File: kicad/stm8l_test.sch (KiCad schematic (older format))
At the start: 39 parts, among them J1 Conn_01x04, J2 Conn_01x02, SW1 SW_Push, SW2 Rotary_Encoder_Switch, U1 STM8L101F3P

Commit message: stuff
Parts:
- BZ1: renamed from BZ?; footprint (none) -> Buzzer_Beeper:Buzzer_12x9.5RM7.6
- C1, C4: renamed from C?; footprint (none) -> Capacitor_SMD:C_0805_2012Metric_Pad1.18x1.45mm_HandSolder
- C2: renamed from C1; footprint (none) -> Capacitor_SMD:C_0603_1608Metric_Pad1.08x0.95mm_HandSolder
- C3: renamed from C2; footprint (none) -> Capacitor_SMD:C_0805_2012Metric_Pad1.18x1.45mm_HandSolder
- D1: renamed from D8; footprint (none) -> LED_SMD:LED_1206_3216Metric_Pad1.42x1.75mm_HandSolder
- D10: renamed from D?; footprint (none) -> LED_SMD:LED_1206_3216Metric_Pad1.42x1.75mm_HandSolder
- D2: renamed from D1; footprint (none) -> LED_SMD:LED_1206_3216Metric_Pad1.42x1.75mm_HandSolder
- D3: renamed from D2; footprint (none) -> LED_SMD:LED_1206_3216Metric_Pad1.42x1.75mm_HandSolder
- D4: renamed from D3; footprint (none) -> LED_SMD:LED_1206_3216Metric_Pad1.42x1.75mm_HandSolder
- D5: renamed from D4; footprint (none) -> LED_SMD:LED_1206_3216Metric_Pad1.42x1.75mm_HandSolder
- D6: renamed from D?; footprint (none) -> Diode_SMD:D_1210_3225Metric_Pad1.42x2.65mm_HandSolder
- D7: renamed from D5; footprint (none) -> LED_SMD:LED_1206_3216Metric_Pad1.42x1.75mm_HandSolder
- D8: renamed from D6; footprint (none) -> LED_SMD:LED_1206_3216Metric_Pad1.42x1.75mm_HandSolder
- D9: renamed from D7; footprint (none) -> LED_SMD:LED_1206_3216Metric_Pad1.42x1.75mm_HandSolder
- J1: footprint (none) -> Connector_PinHeader_2.54mm:PinHeader_1x04_P2.54mm_Vertical
- J2: footprint (none) -> TerminalBlock_Phoenix:TerminalBlock_Phoenix_PT-1,5-2-5.0-H_1x02_P5.00mm_Horizontal
- J3: renamed from J?; symbol Connector:USB_B_Micro -> stm8l_test-rescue:USB_B_Micro-Connector
- J4: renamed from J?; footprint (none) -> Connector_PinHeader_2.00mm:PinHeader_1x02_P2.00mm_Vertical
- L1: renamed from L?; footprint (none) -> Inductor_SMD:L_Wuerth_WE-PD-Typ-7345
- R1: footprint (none) -> Resistor_SMD:R_0603_1608Metric_Pad0.98x0.95mm_HandSolder
- R10: renamed from R7; footprint (none) -> Resistor_SMD:R_0603_1608Metric_Pad0.98x0.95mm_HandSolder
- R11: renamed from R8; footprint (none) -> Resistor_SMD:R_0603_1608Metric_Pad0.98x0.95mm_HandSolder
- R12, R2, R8: renamed from R?; footprint (none) -> Resistor_SMD:R_0603_1608Metric_Pad0.98x0.95mm_HandSolder
- R3: renamed from R9; footprint (none) -> Resistor_SMD:R_0603_1608Metric_Pad0.98x0.95mm_HandSolder
- R4: renamed from R2; footprint (none) -> Resistor_SMD:R_0603_1608Metric_Pad0.98x0.95mm_HandSolder
- R5: renamed from R3; footprint (none) -> Resistor_SMD:R_0603_1608Metric_Pad0.98x0.95mm_HandSolder
- R6: renamed from R4; footprint (none) -> Resistor_SMD:R_0603_1608Metric_Pad0.98x0.95mm_HandSolder
- R7: renamed from R5; footprint (none) -> Resistor_SMD:R_0603_1608Metric_Pad0.98x0.95mm_HandSolder
- R9: renamed from R6; footprint (none) -> Resistor_SMD:R_0603_1608Metric_Pad0.98x0.95mm_HandSolder
- SW1: footprint (none) -> Button_Switch_THT:SW_PUSH_6mm
- SW2: renamed from SW?; footprint (none) -> Connector_PinSocket_2.54mm:PinSocket_1x03_P2.54mm_Vertical
- SW3: renamed from SW2; footprint (none) -> Rotary_Encoder:RotaryEncoder_Alps_EC11E-Switch_Vertical_H20mm
- U3: renamed from U?; symbol random_things:BD70522GUL-E2 -> stm8l_test-rescue:BD70522GUL-E2-random_things
- gave numbers to parts that had none: 2
- renumbered U1 to U2
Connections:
- wire segments 29 -> 30
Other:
- moved on the sheet: BZ1, C1, C2, C3, C4, D1, D10, D2, D3, D4, D5, D6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

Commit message: Rev1 deb pcb
eta ets not stronk
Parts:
- removed D1: green, LED_SMD:LED_1206_3216Metric_Pad1.42x1.75mm_HandSolder, symbol Device:LED_Small
- removed J3: USB_B_Micro, symbol stm8l_test-rescue:USB_B_Micro-Connector
- removed J4: bat, Connector_PinHeader_2.00mm:PinHeader_1x02_P2.00mm_Vertical, symbol Connector_Generic:Conn_01x02
- removed R10, R11, R12, R4, R5, R6, R7, R9: 330, Resistor_SMD:R_0603_1608Metric_Pad0.98x0.95mm_HandSolder, symbol Device:R_Small
- removed R3: 1k, Resistor_SMD:R_0603_1608Metric_Pad0.98x0.95mm_HandSolder, symbol Device:R_Small
- removed U1: MCP73832-2-OT, Package_TO_SOT_SMD:SOT-23-5, symbol Battery_Management:MCP73832-2-OT
- removed U3: BD70522GUL-E2, symbol stm8l_test-rescue:BD70522GUL-E2-random_things
- added U3: BD70522GUL-E2, good_things:BGA-9_3x3_1.76x1.56mm, symbol good_things:BD70522GUL-E2
- BZ1: footprint Buzzer_Beeper:Buzzer_12x9.5RM7.6 -> good_things:buzzer_d14_p5
- C1, C3, C4: footprint Capacitor_SMD:C_0805_2012Metric_Pad1.18x1.45mm_HandSolder -> Capacitor_SMD:C_0805_2012Metric_Pad1.15x1.40mm_HandSolder
- C2: footprint Capacitor_SMD:C_0603_1608Metric_Pad1.08x0.95mm_HandSolder -> Capacitor_SMD:C_0603_1608Metric_Pad1.05x0.95mm_HandSolder
- R1: value R_Small -> 10k; footprint Resistor_SMD:R_0603_1608Metric_Pad0.98x0.95mm_HandSolder -> Resistor_SMD:R_0603_1608Metric_Pad1.05x0.95mm_HandSolder
- R2: value 2k -> 1k; footprint Resistor_SMD:R_0603_1608Metric_Pad0.98x0.95mm_HandSolder -> Resistor_SMD:R_0603_1608Metric_Pad1.05x0.95mm_HandSolder
- R8: footprint Resistor_SMD:R_0603_1608Metric_Pad0.98x0.95mm_HandSolder -> Resistor_SMD:R_0603_1608Metric_Pad1.05x0.95mm_HandSolder
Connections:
- net labels added: 1v8
- net labels removed: +5V, 2v5, charge
- wire segments 30 -> 27
- no-connect marks 9 -> 5
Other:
- moved on the sheet: BZ1, D10, D2, D3, D4, D5, D6, D7, D8, D9, Q1, R8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

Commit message: thinking about the solution, picking leds et al
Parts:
- removed C1: 10u, Capacitor_SMD:C_0805_2012Metric_Pad1.15x1.40mm_HandSolder, symbol Device:C_Small
- removed C4: 22u, Capacitor_SMD:C_0805_2012Metric_Pad1.15x1.40mm_HandSolder, symbol Device:C_Small
- removed D10, D8, D9: red, LED_SMD:LED_1206_3216Metric_Pad1.42x1.75mm_HandSolder, symbol Device:LED_Small
- removed L1: 2u2, Inductor_SMD:L_Wuerth_WE-PD-Typ-7345, symbol Device:L_Small
- removed R1: 10k, Resistor_SMD:R_0603_1608Metric_Pad1.05x0.95mm_HandSolder, symbol Device:R_Small
- removed U3: BD70522GUL-E2, good_things:BGA-9_3x3_1.76x1.56mm, symbol good_things:BD70522GUL-E2
- added D? (x20): red, LED_SMD:LED_1206_3216Metric_Pad1.42x1.75mm_HandSolder, symbol Device:LED_Small
- added F?: 500ma, symbol Device:Fuse_Small
- added Q? (x6): SI2365EDS-T1-GE3, symbol Device:Q_PMOS_GSD
- added R?: 1k, symbol Device:R_Small
- D7: value red -> VLMO30L1M2-GS18
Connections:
- net labels added: a0, a1, a2, a3, a4, c0, c1, c2, c3, c4, c5, pa0
- net labels removed: 1v8, b0, b1, b2, b3, b4, b5, b6, b7, encoder_sw, swim_data
- wire segments 27 -> 88
- no-connect marks 5 -> 2
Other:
- moved on the sheet: BZ1, C2, C3, D2, D3, D4, D5, D6, D7, J1, J2, Q1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

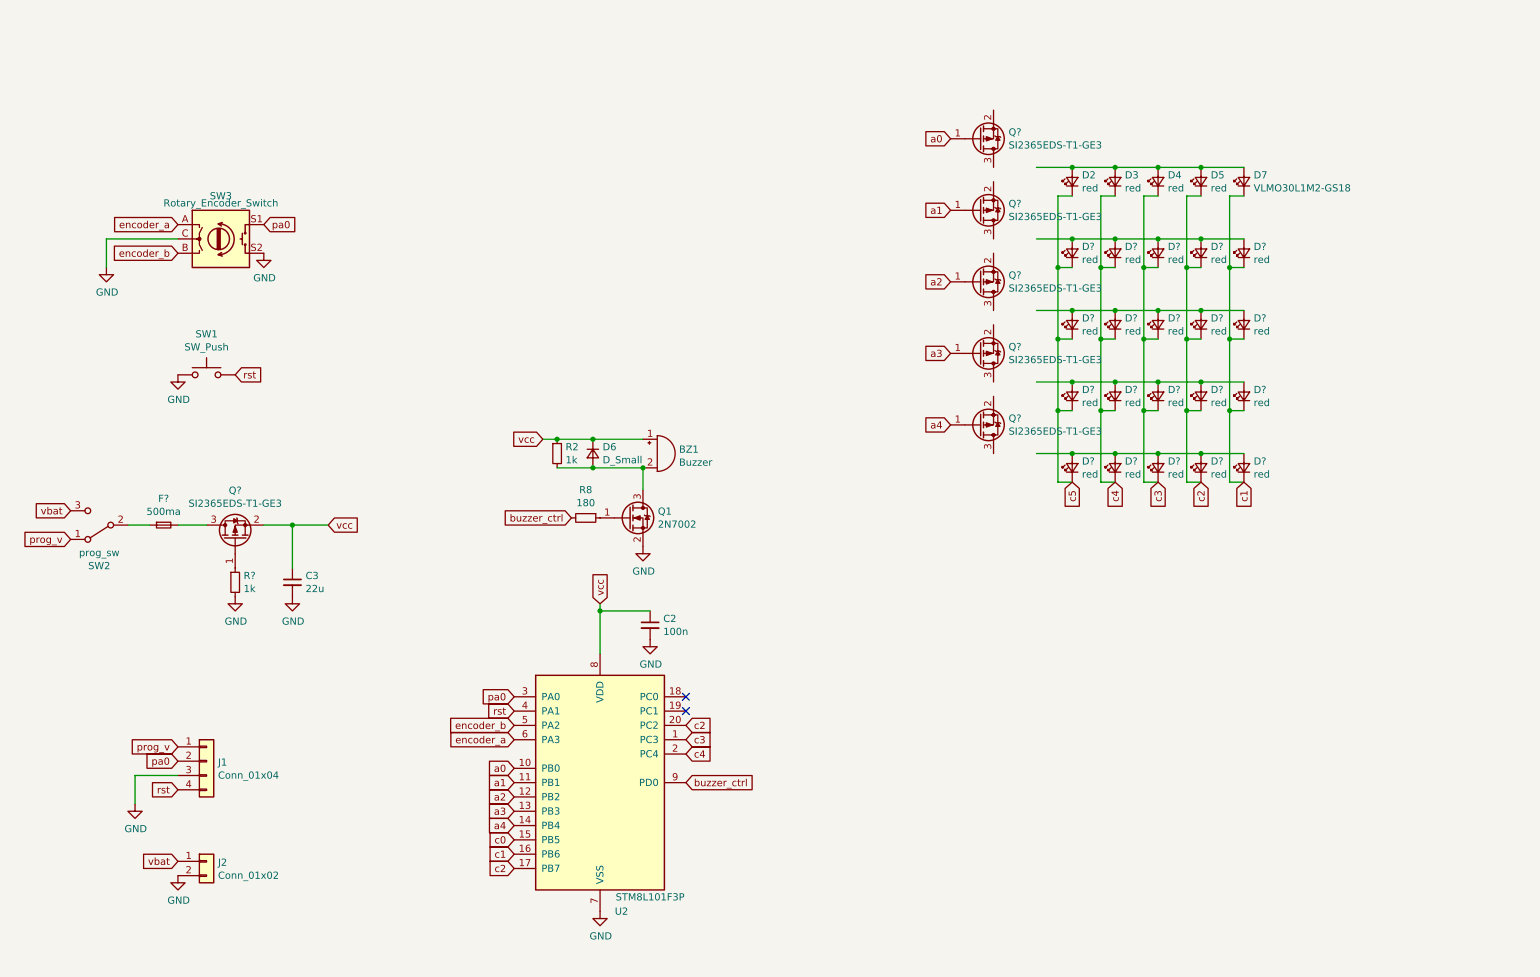
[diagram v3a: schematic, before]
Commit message: Pdb work, schema done
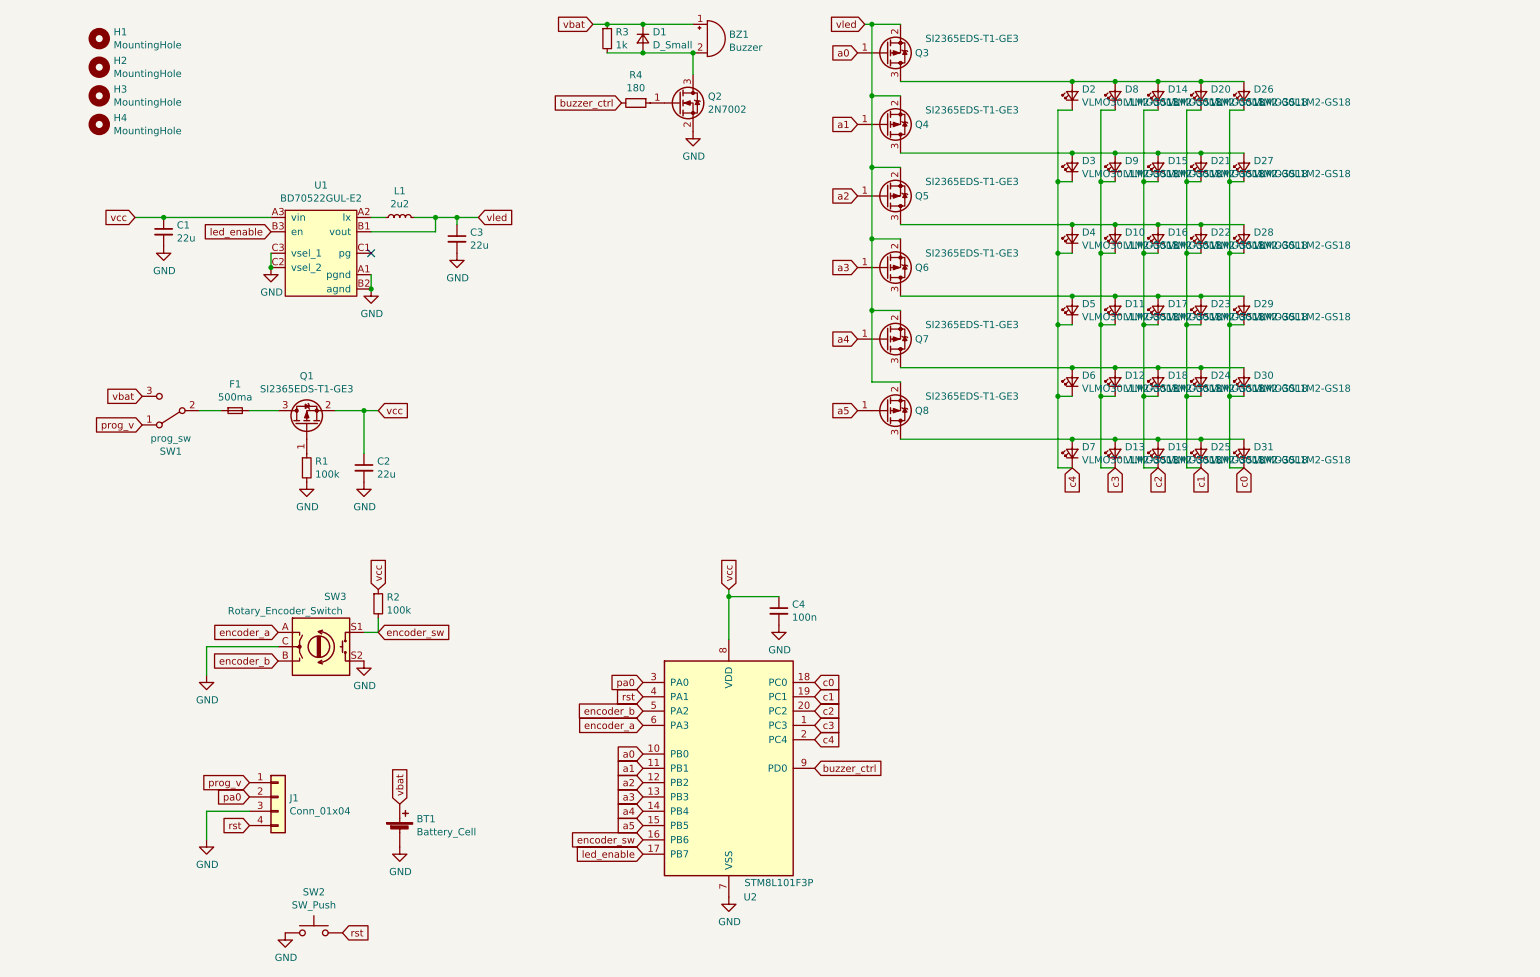
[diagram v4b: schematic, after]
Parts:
- removed D? (x20): red, LED_SMD:LED_1206_3216Metric_Pad1.42x1.75mm_HandSolder, symbol Device:LED_Small
- removed J2: Conn_01x02, TerminalBlock_Phoenix:TerminalBlock_Phoenix_PT-1,5-2-5.0-H_1x02_P5.00mm_Horizontal, symbol Connector_Generic:Conn_01x02
- removed Q? (x5): SI2365EDS-T1-GE3, symbol Device:Q_PMOS_GSD
- added BT1: Battery_Cell, Battery:BatteryHolder_Keystone_3002_1x2032, symbol Device:Battery_Cell
- added C1, C3: 22u, Capacitor_SMD:C_0603_1608Metric_Pad1.05x0.95mm_HandSolder, symbol Device:C_Small
- added D10, D11, D12, D13, D14, D15, D16, D17, D18, D19, D20, D21, D22, D23, D24, D25, D27, D28, D29, D30, D31, D6, D7, D8, D9: VLMO30L1M2-GS18, LED_SMD:LED_PLCC-2, symbol Device:LED_Small
- added H1, H2, H3, H4: MountingHole, MountingHole:MountingHole_2.7mm_M2.5, symbol Mechanical:MountingHole
- added L1: 2u2, Inductor_SMD:L_Wuerth_WE-PD-Typ-7345, symbol Device:L_Small
- added Q3, Q4, Q5, Q6, Q7, Q8: SI2365EDS-T1-GE3, Package_TO_SOT_SMD:SOT-23_Handsoldering, symbol Device:Q_PMOS_GSD
- added R2: 100k, Resistor_SMD:R_0603_1608Metric_Pad1.05x0.95mm_HandSolder, symbol Device:R_Small
- added U1: BD70522GUL-E2, good_things:BGA-9_3x3_1.76x1.56mm, symbol good_things:BD70522GUL-E2
- C2: renamed from C3; footprint Capacitor_SMD:C_0805_2012Metric_Pad1.15x1.40mm_HandSolder -> Capacitor_SMD:C_0603_1608Metric_Pad1.05x0.95mm_HandSolder
- D2, D3, D4, D5: value red -> VLMO30L1M2-GS18; footprint LED_SMD:LED_1206_3216Metric_Pad1.42x1.75mm_HandSolder -> LED_SMD:LED_PLCC-2
- D26: renamed from D7; footprint LED_SMD:LED_1206_3216Metric_Pad1.42x1.75mm_HandSolder -> LED_SMD:LED_PLCC-2
- F1: renamed from F?; footprint (none) -> Fuse:Fuse_1206_3216Metric_Pad1.42x1.75mm_HandSolder
- J1: footprint Connector_PinHeader_2.54mm:PinHeader_1x04_P2.54mm_Vertical -> good_things:TSM-104-01-L-SH
- Q1: renamed from Q?; footprint (none) -> Package_TO_SOT_SMD:SOT-23_Handsoldering
- R1: renamed from R?; value 1k -> 100k; footprint (none) -> Resistor_SMD:R_0603_1608Metric_Pad1.05x0.95mm_HandSolder
- SW1: renamed from SW2; footprint Connector_PinSocket_2.54mm:PinSocket_1x03_P2.54mm_Vertical -> good_things:TSM-103-01-l_SH
- SW2: renamed from SW1; footprint Button_Switch_THT:SW_PUSH_6mm -> good_things:push_sw_purple
- renumbered C2 to C4, D6 to D1, Q1 to Q2, R2 to R3, R8 to R4
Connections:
- net labels added: a5, encoder_sw, led_enable, vled
- net labels removed: c5
- wire segments 88 -> 128
- no-connect marks 2 -> 1
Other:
- moved on the sheet: BZ1, C2, C4, D1, D26, F1, J1, Q1, Q2, R1, R3, R4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

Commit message: Place components and initial routing
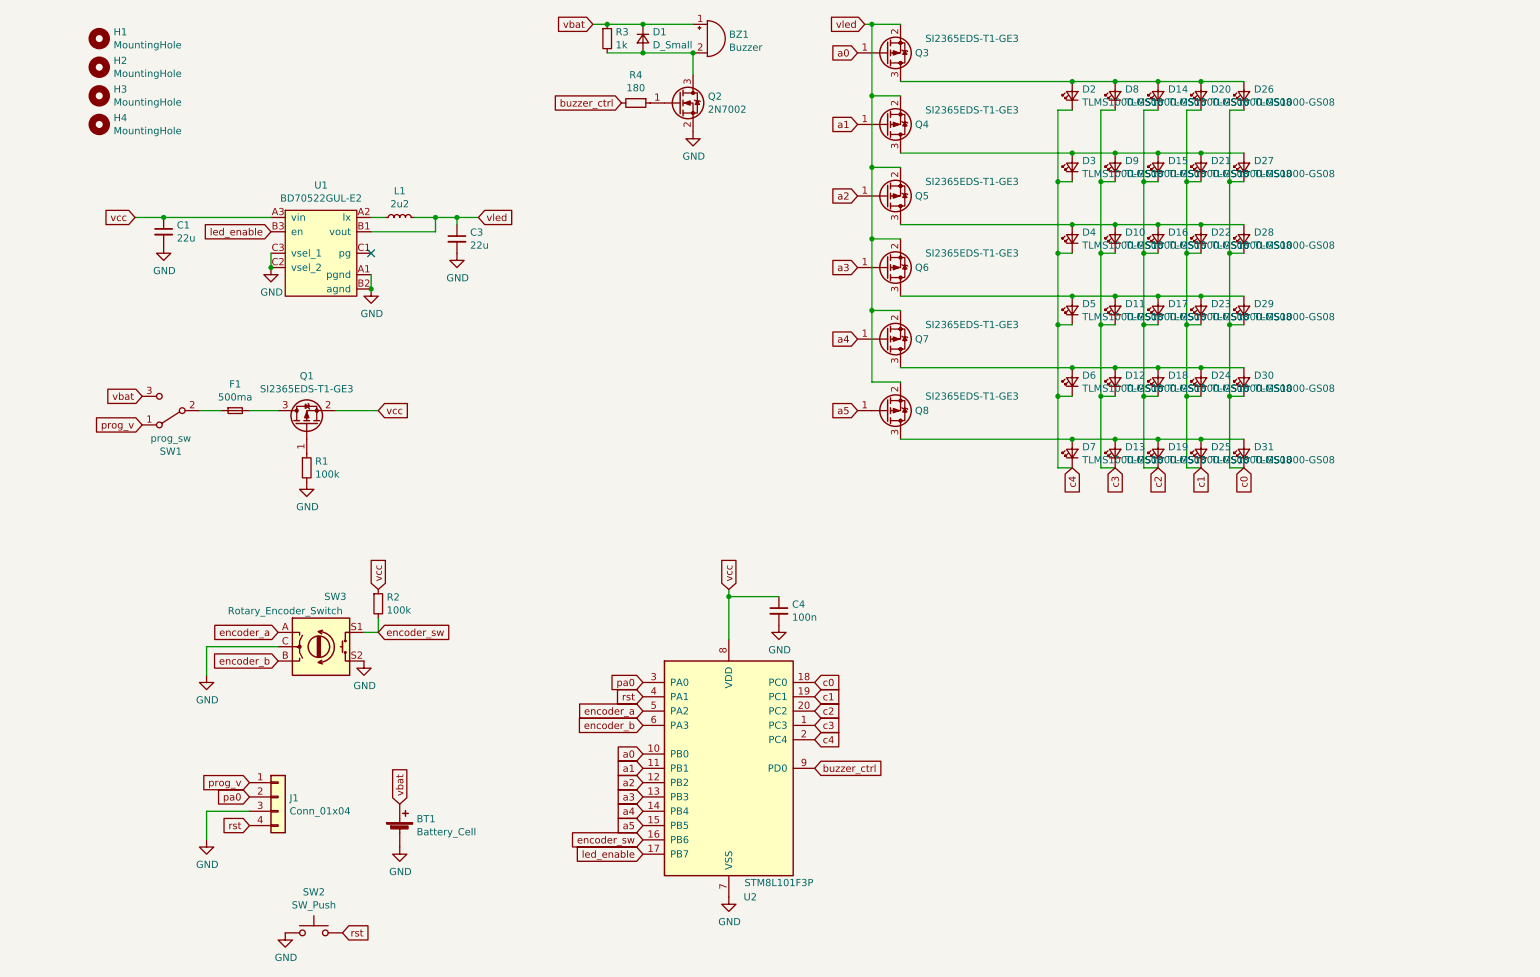
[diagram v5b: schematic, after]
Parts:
- removed C2: 22u, Capacitor_SMD:C_0603_1608Metric_Pad1.05x0.95mm_HandSolder, symbol Device:C_Small
- D10, D11, D12, D13, D14, D15, D16, D17, D18, D19, D2, D20, D21, D22, D23, D24, D25, D26, D27, D28, D29, D3, D30, D31, D4, D5, D6, D7, D8, D9: value VLMO30L1M2-GS18 -> TLMS1000-GS08; footprint LED_SMD:LED_PLCC-2 -> LED_SMD:LED_0603_1608Metric_Pad1.05x0.95mm_HandSolder
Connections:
- net encoder_a: now also U2.5 (PA2); no longer U2.6 (PA3)
- net encoder_b: now also U2.6 (PA3); no longer U2.5 (PA2)
